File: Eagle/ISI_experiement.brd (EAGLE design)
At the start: 100 x 80 mm, 13 parts, among them IC2 74AC04N, J5 JP2, U2 7486*

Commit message: merge power
needs more work just uploaded to save progress
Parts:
- removed IC2: 74AC04N, E3VB_ISI:14-DIP
- removed J5, J_CAP, J_IN, J_TL: JP2, E3VB_ISI:JP2
- removed U1: (no value), E3VB_ISI:20-DIP
- removed U2: 7486*, E3VB_ISI:14-DIP
- added C2, C4, C5, C9: 100uF, adafruit:C1206K
- added C3, C8: 10uF, adafruit:C1206K
- added C6: 0.1uF, adafruit:C1206K
- added C7: 18pF, adafruit:C1206K
- added IC1, IC3, IC4: 74AC11374D, 74ac-logic:SO24W
- added IC5, IC6: 74266D, 74xx-us:SO14
- added IC7: 74HC04D, 74xx-eu:SO14
- added JP1, JP2, JP3, JP4: (no value), jumper:JP1
- added LED1: (no value), adafruit:CHIPLED_0805
- added R1: 1K, adafruit:R0805
- added R2: 51K, adafruit:R0805
- added R3: 30K, adafruit:R0805
- added R4: 220, adafruit:R0805
- added SJ1, SJ2: (no value), jumper:SJW
- added U$1: TPS796, Capstone:TPS796
- added USBMINI: (no value), adafruit:USB-MINIB
- C1: device resistor:CTRIM3050.504 -> c-trimm:3008
- L1: value RF_INDUCTOR -> SMF51-2-51-15; device E3VB_ISI:ADJ_IND_NON_STD_PKG -> inductor-neosid:SMF5_1
- moved L1 292.5 mm to (-33.0, -217.0), turned to 0 degrees
- moved C1 247.9 mm to (-43.0, -217.0), turned to 0 degrees
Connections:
- removed net GNDA: C_GND.1, IC2.7, J_CAP.1, U1.10, U1.12, U1.13, U1.14, U1.15, U1.16, U1.17, U1.3, U1.4, U1.5, U1.6, U1.7, U1.8, U1.9, U2.7
- removed net J_TL: IC2.3, J5.1, J_TL.2, TP$2.1
- removed net N$7: U1.19, U2.1
- removed net N$9: U1.2, U2.3
- new net A0: IC3.1, IC3.22
- new net A1: IC3.2, IC3.21
- new net A2: IC3.20
- new net A3: IC3.3, IC5.8
- new net A4: IC3.23, IC3.4, IC3.9, IC5.10, IC5.9
- new net A5: IC3.10
- new net A6: IC3.11, IC5.12
- new net FB0: IC1.23, IC5.3
- new net FB1: IC5.4
- new net GND: C3.2, C4.2, C5.2, C6.2, C8.2, C9.2, C_GND.1, IC1.5, IC1.6, IC1.7, IC1.8, IC3.5, IC3.6, IC3.7, IC3.8, IC4.5, IC4.6, IC4.7, IC4.8, IC5.7, IC6.7, IC7.7, JP2.1, R3.1, R4.1, SJ1.1, SJ2.1, U$1.6, U$1.GND, USBMINI.GND
- new net JNC: C7.1, C8.1, C9.1, LED1.A, R2.2, SJ2.2, U$1.OUT
- new net N$10: R1.2, U$1.EN
- new net N$12: C7.2, R2.1, R3.2, U$1.NR/FB
- new net N$13: LED1.C, R4.2
- new net N$15: IC1.4, IC5.2
- new net N$17: IC7.4, TP3.1
- new net N$18: C1.-, JP2.2
- new net N$27: IC3.12, IC5.13
- new net N$28: IC4.2, IC6.1
- new net N$29: IC4.3, IC6.2
- new net N$5: C2.1, C3.1, C4.1, C5.1, C6.1, IC7.14, R1.1, SJ1.2, U$1.IN, USBMINI.VBUS
- new net Q0: IC1.1, IC1.22
- new net Q1: IC1.2, IC1.21
- new net Q2: IC1.20, IC1.3, IC5.1
- new net Q4: IC1.16, IC1.9
- new net Q5: IC1.10, IC1.15
- new net Q6: IC1.11, IC1.14, IC5.5
- net N$1: now also JP3.2, L1.1; no longer IC2.1, J_IN.2
- net N$2: now also IC7.1, JP4.2; no longer J5.2, L1.P$2
- net N$3: now also C1.+, IC7.2, JP1.1, L1.5; no longer C1.1, IC2.2, J_TL.1, L1.P$3
- net N$4: now also IC7.3, JP1.2, JP3.1, TP$2.1; no longer IC2.4, TP3.1
- net N$6: now also JP4.1; no longer C1.2, J_CAP.2
- net N$8: now also IC1.12, IC5.6; no longer U1.18, U2.2
- net VCC: now also IC1.18, IC1.19, IC3.18, IC3.19, IC4.18, IC4.19, IC5.14, IC6.14; no longer IC2.14, U1.20, U2.14
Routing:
- net GNDA: track 178.8 -> 0.00 mm
- net N$3: track 90.5 -> 0.00 mm
- net J_TL: track 88.7 -> 0.00 mm
- net N$9: track 71.6 -> 0.00 mm
- net N$8: track 55.8 -> 0.00 mm
- net N$7: track 47.1 -> 0.00 mm
- net N$2: track 22.7 -> 0.00 mm
- net N$4: track 19.6 -> 0.00 mm
- net N$1: track 14.3 -> 0.00 mm
- net N$6: track 3.85 -> 0.00 mm

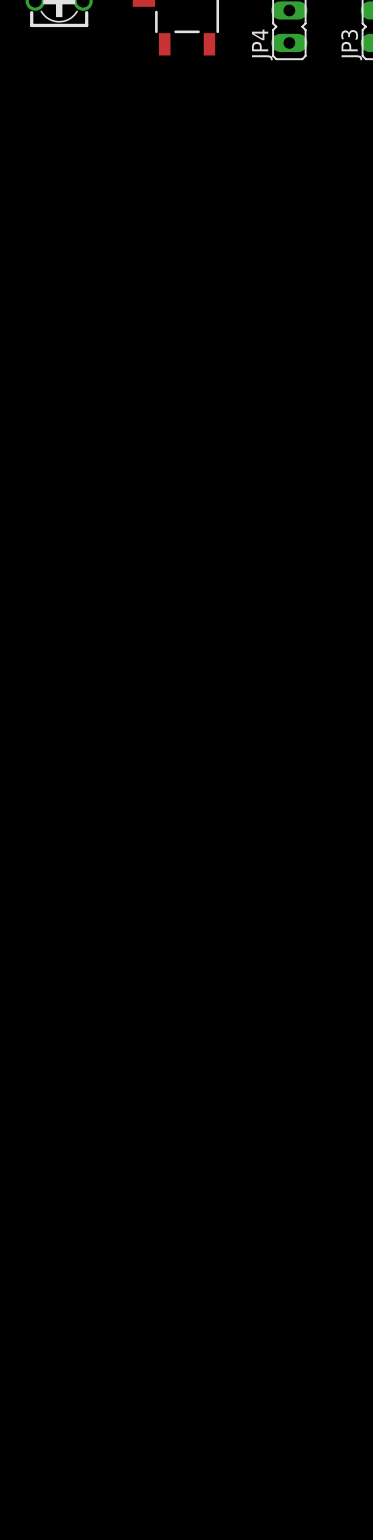
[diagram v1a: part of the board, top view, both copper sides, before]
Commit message: added aggressor and LFSR
need to add a clock and review a inductor part and schematic
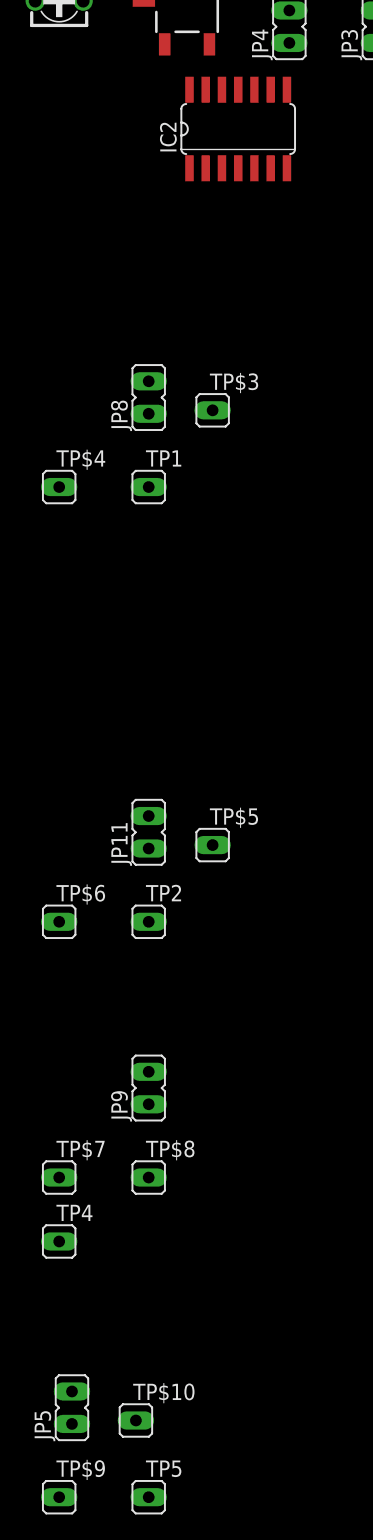
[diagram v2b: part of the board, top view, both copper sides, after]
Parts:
- added IC2: 74HC04D, 74xx-eu:SO14
- added JP11, JP5, JP8, JP9: (no value), jumper:JP1
- added TP$10, TP$3, TP$4, TP$5, TP$6, TP$7, TP$8, TP$9, TP1, TP2, TP4, TP5: JP1, E3VB_ISI:JP1
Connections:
- net N$8 renamed O_LFSR1
- removed net A3: IC3.3, IC5.8
- removed net A6: IC3.11, IC5.12
- removed net N$15: IC1.4, IC5.2
- removed net N$27: IC3.12, IC5.13
- removed net N$28: IC4.2, IC6.1
- removed net N$29: IC4.3, IC6.2
- removed net N$5: C2.1, C3.1, C4.1, C5.1, C6.1, IC7.14, R1.1, SJ1.2, U$1.IN, USBMINI.VBUS
- removed net N$6: JP4.1
- new net B0: IC4.1, IC4.22
- new net B1: IC4.2, IC4.21, IC6.1
- new net B4: IC4.16, IC4.9
- new net B6: IC4.11, IC4.14
- new net FB2: IC3.23, IC4.17, IC5.10
- new net FB3: IC3.17, IC4.15, IC5.11
- new net FB4: IC4.23, IC6.3
- new net N$11: IC2.6, IC2.9, TP$5.1, TP$6.1
- new net N$14: IC2.1, JP8.2
- new net N$16: IC2.10, IC2.13, TP$7.1, TP$8.1
- new net N$19: IC7.8, TP5.1
- new net N$20: IC2.8, TP2.1
- new net N$21: IC7.5, JP5.2
- new net N$22: IC2.5, JP11.2
- new net N$24: IC2.12, TP4.1
- new net N$25: IC2.11, JP9.2
- new net N$7: IC2.2, IC2.3, TP$3.1, TP$4.1
- new net N$8: IC7.6, IC7.9, TP$10.1, TP$9.1
- new net N$9: IC2.4, TP1.1
- new net O_LFSR2: IC3.4, IC5.9
- new net O_LSFR3: IC3.11, IC5.13
- new net TT_A1: IC1.4, IC5.2, JP8.1
- new net TT_A2: IC4.4, JP11.1
- new net TT_A3: IC4.12, JP9.1
- new net TT_A4: IC4.3, IC6.2, JP5.1
- new net TT_V: IC4.10, JP4.1
- new net VCC-5V: IC6.14
- new net VCC_5V: C2.1, C3.1, C4.1, C5.1, C6.1, IC1.19, IC2.14, IC3.19, IC4.19, IC5.14, IC7.14, R1.1, SJ1.2, U$1.IN, USBMINI.VBUS
- net A2: now also IC3.3, IC5.8
- net A4: now also IC3.16; no longer IC3.23, IC3.4, IC5.10, IC5.9
- net A5: now also IC3.15, IC5.12
- net FB1: now also IC1.17, IC4.20
- net GND: now also IC2.7, IC3.12, IC3.14
- net VCC: no longer IC1.19, IC3.19, IC4.19, IC5.14, IC6.14

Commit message: new MSGP
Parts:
- added COUNTER: 74HC191N, 74xx-eu:DIL16
- added DEL: 74AC11240D, 74ac-logic:SO24W
- added JP6: (no value), adafruit:2X04
- added RC1: 1K, adafruit:R0805
- added RC2, RC3, RC4, RC5, RC6, RC7, RC8, RC9: 15, adafruit:R0805
- added U$2: ECS-8FX, Capstone:ECS-8FX
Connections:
- new net CLK1: IC1.13, RC6.1
- new net CLK2: IC3.13, RC7.1
- new net CLK3: IC4.13, RC8.1
- new net CLK4: RC9.1
- new net N$15: COUNTER.3, RC2.2
- new net N$23: COUNTER.2, RC3.2
- new net N$26: COUNTER.6, RC4.2
- new net N$27: COUNTER.7, RC5.2
- new net N$28: JP6.1, RC2.1
- new net N$29: JP6.5, RC4.1
- new net N$30: JP6.3, RC3.1
- new net N$31: JP6.7, RC5.1
- new net N$32: DEL.20, DEL.21, DEL.22, DEL.23, JP6.2, JP6.4, JP6.6, JP6.8
- new net N$33: DEL.1, RC6.2
- new net N$34: DEL.2, RC7.2
- new net N$35: DEL.3, RC8.2
- new net N$36: DEL.4, RC9.2
- new net N$5: RC1.1, U$2.TRI-STATE
- new net N$6: COUNTER.14, U$2.OUTPUT
- net GND: now also COUNTER.1, COUNTER.10, COUNTER.15, COUNTER.4, COUNTER.5, COUNTER.8, COUNTER.9, DEL.24, DEL.5, DEL.6, DEL.7, DEL.8, U$2.GND
- net VCC: now also COUNTER.11, COUNTER.16, DEL.18, DEL.19, RC1.2, U$2.VCC
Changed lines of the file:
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@@
 <element name="TP$10" library="E3VB_ISI" package="JP1" value="JP1" x="-37" y="-328"/>
 <element name="JP5" library="jumper" package="JP1" value="" x="-42" y="-327"/>
+<element name="U$2" library="Capstone" package="ECS-8FX" value="ECS-8FX" x="-45" y="-337"/>
+<element name="COUNTER" library="74xx-eu" package="DIL16" value="74HC191N" x="-33" y="-355"/>
+<element name="DEL" library="74ac-logic" package="SO24W" value="74AC11240D" x="-36" y="-368"/>
+<element name="RC1" library="adafruit" package="R0805" value="1K" x="-16" y="-377"/>
+<element name="JP6" library="adafruit" package="2X04" value="" x="-22" y="-366"/>
+<element name="RC2" library="adafruit" package="R0805" value="15" x="-44" y="-383"/>
+<element name="RC3" library="adafruit" package="R0805" value="15" x="-38" y="-383"/>
+<element name="RC4" library="adafruit" package="R0805" value="15" x="-32" y="-383"/>
+<element name="RC5" library="adafruit" package="R0805" value="15" x="-26" y="-383"/>
+<element name="RC6" library="adafruit" package="R0805" value="15" x="-20" y="-383"/>
+<element name="RC7" library="adafruit" package="R0805" value="15" x="-14" y="-383"/>
+<element name="RC8" library="adafruit" package="R0805" value="15" x="-44" y="-389"/>
+<element name="RC9" library="adafruit" package="R0805" value="15" x="-38" y="-389"/>
 </elements>
 <signals>
@@
 <contactref element="IC3" pad="18"/>
 <contactref element="IC4" pad="18"/>
-<wire x1="96.52" y1="26.67" x2="96.52" y2="26.67" width="0" layer="19" extent="1-16"/>
+<contactref element="COUNTER" pad="16"/>
+<contactref element="DEL" pad="18"/>
+<contactref element="DEL" pad="19"/>
+<contactref element="RC1" pad="2"/>
+<contactref element="COUNTER" pad="11"/>
+<contactref element="U$2" pad="VCC"/>
+<wire x1="-35.365" y1="-362.9708" x2="-36.635" y2="-362.9708" width="0" layer="19" extent="1-1"/>
+<wire x1="-41.89" y1="-351.19" x2="-36.635" y2="-362.9708" width="0" layer="19" extent="1-1"/>
+<wire x1="-29.19" y1="-351.19" x2="-41.89" y2="-351.19" width="0" layer="19" extent="1-1"/>
+<wire x1="-40.5" y1="-336" x2="-41.89" y2="-351.19" width="0" layer="19" extent="1-1"/>
+<wire x1="-15" y1="-377" x2="-35.365" y2="-362.9708" width="0" layer="19" extent="1-1"/>
+<wire x1="10.635" y1="-63.9708" x2="-40.5" y2="-336" width="0" layer="19" extent="1-1"/>
+<wire x1="10.635" y1="-50.9708" x2="10.635" y2="-63.9708" width="0" layer="19" extent="1-1"/>
+<wire x1="10.635" y1="-37.9708" x2="10.635" y2="-50.9708" width="0" layer="19" extent="1-1"/>
+<wire x1="25.4" y1="34.29" x2="10.635" y2="-37.9708" width="0" layer="19" extent="1-1"/>
 <wire x1="25.4" y1="34.29" x2="25.4" y2="34.29" width="0" layer="19" extent="1-16"/>
-<wire x1="10.635" y1="-37.9708" x2="25.4" y2="34.29" width="0" layer="19" extent="1-16"/>
-<wire x1="10.635" y1="-50.9708" x2="10.635" y2="-37.9708" width="0" layer="19" extent="1-1"/>
-<wire x1="10.635" y1="-63.9708" x2="10.635" y2="-50.9708" width="0" layer="19" extent="1-1"/>
+<wire x1="88.9" y1="26.67" x2="88.9" y2="26.67" width="0" layer="19" extent="1-16"/>
 </signal>
 <signal name="GND">
@@
 <contactref element="IC4" pad="8"/>
 <contactref element="IC3" pad="8"/>
+<contactref element="COUNTER" pad="8"/>
+<contactref element="DEL" pad="5"/>
+<contactref element="DEL" pad="6"/>
+<contactref element="DEL" pad="7"/>
+<contactref element="DEL" pad="8"/>
+<contactref element="COUNTER" pad="15"/>
+<contactref element="COUNTER" pad="1"/>
+<contactref element="COUNTER" pad="10"/>
+<contactref element="COUNTER" pad="9"/>
+<contactref element="COUNTER" pad="4"/>
+<contactref element="COUNTER" pad="5"/>
+<contactref element="DEL" pad="24"/>
+<contactref element="U$2" pad="GND"/>
 <wire x1="-11" y1="-220.27" x2="-25.19" y2="-230.0734" width="0" layer="19" extent="1-1"/>
 <wire x1="4.5" y1="-210" x2="-11" y2="-220.27" width="0" layer="19" extent="1-1"/>
@@
 <wire x1="9.365" y1="-48.0292" x2="10.635" y2="-48.0292" width="0" layer="19" extent="1-1"/>
 <wire x1="8.095" y1="-48.0292" x2="9.365" y2="-48.0292" width="0" layer="19" extent="1-1"/>
+<wire x1="-35.5" y1="-348" x2="-25.19" y2="-230.0734" width="0" layer="19" extent="1-1"/>
+<wire x1="-39.35" y1="-351.19" x2="-35.5" y2="-348" width="0" layer="19" extent="1-1"/>
+<wire x1="-41.89" y1="-358.81" x2="-39.35" y2="-351.19" width="0" layer="19" extent="1-1"/>
+<wire x1="-42.985" y1="-362.9708" x2="-41.89" y2="-358.81" width="0" layer="19" extent="1-1"/>
+<wire x1="-34.27" y1="-358.81" x2="-41.89" y2="-358.81" width="0" layer="19" extent="1-1"/>
+<wire x1="-31.73" y1="-358.81" x2="-34.27" y2="-358.81" width="0" layer="19" extent="1-1"/>
+<wire x1="-24.11" y1="-358.81" x2="-31.73" y2="-358.81" width="0" layer="19" extent="1-1"/>
+<wire x1="-24.11" y1="-351.19" x2="-24.11" y2="-358.81" width="0" layer="19" extent="1-1"/>
+<wire x1="-26.65" y1="-351.19" x2="-24.11" y2="-351.19" width="0" layer="19" extent="1-1"/>
+<wire x1="-37.905" y1="-373.0292" x2="-42.985" y2="-362.9708" width="0" layer="19" extent="1-1"/>
+<wire x1="-36.635" y1="-373.0292" x2="-37.905" y2="-373.0292" width="0" layer="19" extent="1-1"/>
+<wire x1="-35.365" y1="-373.0292" x2="-36.635" y2="-373.0292" width="0" layer="19" extent="1-1"/>
+<wire x1="-34.095" y1="-373.0292" x2="-35.365" y2="-373.0292" width="0" layer="19" extent="1-1"/>
 <wire x1="41.91" y1="74.93" x2="11.905" y2="-48.0292" width="0" layer="19" extent="1-1"/>
 </signal>
@@
 <contactref element="IC6" pad="14"/>
 </signal>
+<signal name="N$5">
+<contactref element="U$2" pad="TRI-STATE"/>
+<contactref element="RC1" pad="1"/>
+<wire x1="-40.5" y1="-348" x2="-17" y2="-377" width="0" layer="19" extent="1-1"/>
+</signal>
+<signal name="N$6">
+<contactref element="U$2" pad="OUTPUT"/>
+<contactref element="COUNTER" pad="14"/>
+<wire x1="-35.5" y1="-336" x2="-36.81" y2="-351.19" width="0" layer="19" extent="1-1"/>
+</signal>
+<signal name="N$15">
+<contactref element="COUNTER" pad="3"/>
+<contactref element="RC2" pad="2"/>
+<wire x1="-36.81" y1="-358.81" x2="-43" y2="-383" width="0" layer="19" extent="1-1"/>
+</signal>
+<signal name="N$23">
+<contactref element="COUNTER" pad="2"/>
+<contactref element="RC3" pad="2"/>
+<wire x1="-39.35" y1="-358.81" x2="-37" y2="-383" width="0" layer="19" extent="1-1"/>
+</signal>
+<signal name="N$26">
+<contactref element="COUNTER" pad="6"/>
+<contactref element="RC4" pad="2"/>
+<wire x1="-29.19" y1="-358.81" x2="-31" y2="-383" width="0" layer="19" extent="1-1"/>
+</signal>
+<signal name="N$27">
+<contactref element="COUNTER" pad="7"/>
+<contactref element="RC5" pad="2"/>
+<wire x1="-26.65" y1="-358.81" x2="-25" y2="-383" width="0" layer="19" extent="1-1"/>
+</signal>
+<signal name="N$28">
+<contactref element="RC2" pad="1"/>
+<contactref element="JP6" pad="1"/>
+<wire x1="-25.81" y1="-367.27" x2="-45" y2="-383" width="0" layer="19" extent="1-1"/>
+</signal>
+<signal name="N$29">
+<contactref element="RC4" pad="1"/>
+<contactref element="JP6" pad="5"/>
+<wire x1="-20.73" y1="-367.27" x2="-33" y2="-383" width="0" layer="19" extent="1-1"/>
+</signal>
+<signal name="N$30">
+<contactref element="RC3" pad="1"/>
+<contactref element="JP6" pad="3"/>
+<wire x1="-23.27" y1="-367.27" x2="-39" y2="-383" width="0" layer="19" extent="1-1"/>
+</signal>
+<signal name="N$31">
+<contactref element="RC5" pad="1"/>
+<contactref element="JP6" pad="7"/>
+<wire x1="-18.19" y1="-367.27" x2="-27" y2="-383" width="0" layer="19" extent="1-1"/>
+</signal>
+<signal name="N$32">
+<contactref element="JP6" pad="2"/>
+<contactref element="DEL" pad="20"/>
+<contactref element="JP6" pad="4"/>
+<contactref element="JP6" pad="6"/>
+<contactref element="JP6" pad="8"/>
+<contactref element="DEL" pad="23"/>
+<contactref element="DEL" pad="22"/>
+<contactref element="DEL" pad="21"/>
+<wire x1="-40.445" y1="-362.9708" x2="-41.715" y2="-362.9708" width="0" layer="19" extent="1-1"/>
+<wire x1="-39.175" y1="-362.9708" x2="-40.445" y2="-362.9708" width="0" layer="19" extent="1-1"/>
+<wire x1="-37.905" y1="-362.9708" x2="-39.175" y2="-362.9708" width="0" layer="19" extent="1-1"/>
+<wire x1="-25.81" y1="-364.73" x2="-37.905" y2="-362.9708" width="0" layer="19" extent="1-1"/>
+<wire x1="-23.27" y1="-364.73" x2="-25.81" y2="-364.73" width="0" layer="19" extent="1-1"/>
+<wire x1="-20.73" y1="-364.73" x2="-23.27" y2="-364.73" width="0" layer="19" extent="1-1"/>
+<wire x1="-18.19" y1="-364.73" x2="-20.73" y2="-364.73" width="0" layer="19" extent="1-1"/>
+</signal>
+<signal name="N$33">
+<contactref element="DEL" pad="1"/>
+<contactref element="RC6" pad="2"/>
+<wire x1="-19" y1="-383" x2="-42.985" y2="-373.0292" width="0" layer="19" extent="1-1"/>
+</signal>
+<signal name="N$34">
+<contactref element="DEL" pad="2"/>
+<contactref element="RC7" pad="2"/>
+<wire x1="-13" y1="-383" x2="-41.715" y2="-373.0292" width="0" layer="19" extent="1-1"/>
+</signal>
+<signal name="N$35">
+<contactref element="DEL" pad="3"/>
+<contactref element="RC8" pad="2"/>
+<wire x1="-40.445" y1="-373.0292" x2="-43" y2="-389" width="0" layer="19" extent="1-1"/>
+</signal>
+<signal name="N$36">
+<contactref element="DEL" pad="4"/>
+<contactref element="RC9" pad="2"/>
+<wire x1="-39.175" y1="-373.0292" x2="-37" y2="-389" width="0" layer="19" extent="1-1"/>
+</signal>
+<signal name="CLK4">
+<contactref element="RC9" pad="1"/>
+</signal>
+<signal name="CLK1">
+<contactref element="IC1" pad="13"/>
+<contactref element="RC6" pad="1"/>
+<wire x1="16.985" y1="-37.9708" x2="-21" y2="-383" width="0" layer="19" extent="1-1"/>
+</signal>
+<signal name="CLK2">
+<contactref element="IC3" pad="13"/>
+<contactref element="RC7" pad="1"/>
+<wire x1="16.985" y1="-50.9708" x2="-15" y2="-383" width="0" layer="19" extent="1-1"/>
+</signal>
+<signal name="CLK3">
+<contactref element="IC4" pad="13"/>
+<contactref element="RC8" pad="1"/>
+<wire x1="16.985" y1="-63.9708" x2="-45" y2="-389" width="0" layer="19" extent="1-1"/>
+</signal>
 </signals>

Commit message: really close to final ISI
missing inductor package dimensions and one cap value.
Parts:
- moved C3 272.6 mm to (59.8, 64.7)
- moved C7 272.6 mm to (64.7, 64.7)
- moved C8 272.3 mm to (64.6, 55.2)
- moved C6 271.3 mm to (59.8, 62.5)
- moved C9 262.9 mm to (64.6, 51.6)
- moved R3 261.7 mm to (66.8, 61.5), turned to 270 degrees
- moved C5 261.2 mm to (59.8, 60.2)
- moved R4 260.4 mm to (27.7, 67.6), turned to 270 degrees
- moved C4 259.6 mm to (59.8, 57.5)
- moved R1 258.6 mm to (16.6, 66.6)
- moved C2 258.5 mm to (59.8, 55.3)
- moved USBMINI 258.2 mm to (8.13, 74.2)
- moved U$1 256.8 mm to (57.8, 67.9)
- moved LED1 255.2 mm to (64.6, 57.7), turned to 270 degrees
- moved SJ1 247.8 mm to (59.7, 51.8), turned to 180 degrees
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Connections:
- net JNC renamed VCC_3V
- removed net VCC-5V: IC6.14
- removed net VCC_5V: C2.1, C3.1, C4.1, C5.1, C6.1, IC1.19, IC2.14, IC3.19, IC4.19, IC5.14, IC7.14, R1.1, SJ1.2, U$1.IN, USBMINI.VBUS
- net GND: now also C2.2, IC1.24, IC3.24, IC4.24
- net VCC: now also C2.1, C3.1, C4.1, C5.1, C6.1, IC1.19, IC2.14, IC3.19, IC4.19, IC5.14, IC6.14, IC7.14, R1.1, SJ1.2, U$1.IN, USBMINI.VBUS
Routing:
- net VCC: track 132.7 -> 10.5 mm
- added copper zone on layer 1, net VCC
